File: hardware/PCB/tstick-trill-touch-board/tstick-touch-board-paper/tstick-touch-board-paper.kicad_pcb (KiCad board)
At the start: 2 copper layers, 113.9 x 28 mm, 12 parts

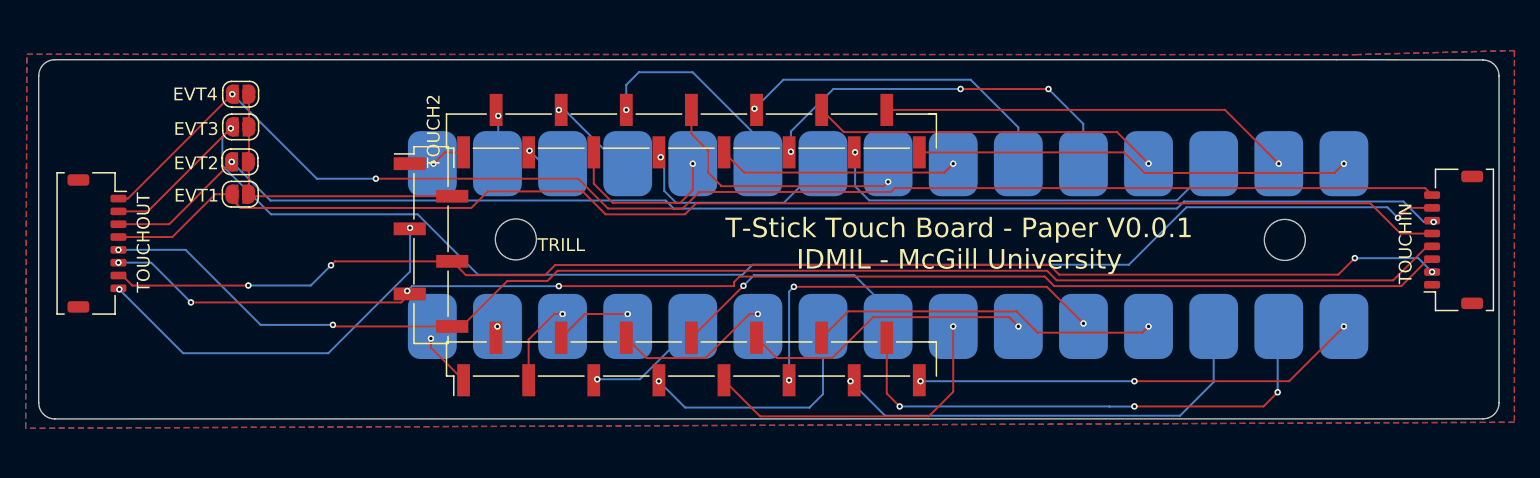
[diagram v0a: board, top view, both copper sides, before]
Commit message: cleaned up the pcb designs for the touch extension boards, created BOM and gerber files for fabrication and assembly
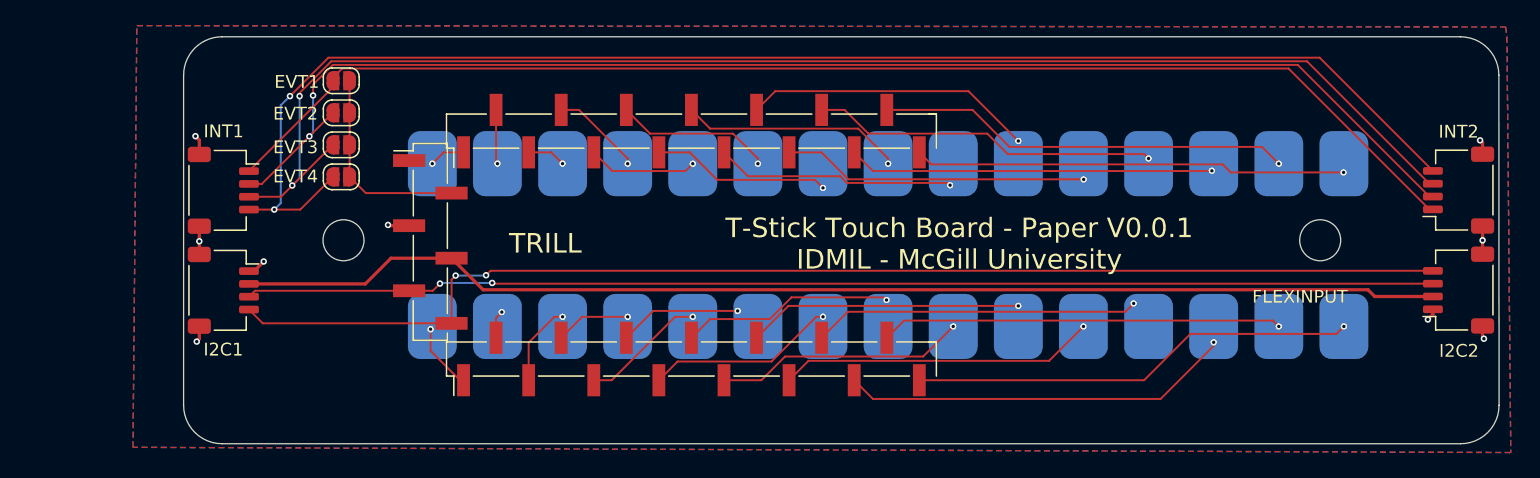
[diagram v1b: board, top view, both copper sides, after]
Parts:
- removed TrillExtensionInput1, TrillExtensionOutput2: Conn_01x08, Connector_JST:JST_SHL_SM08B-SHLS-TF_1x08-1MP_P1.00mm_Horizontal
- added I2C1: Conn_01x04, Connector_JST:JST_SH_SM04B-SRSS-TB_1x04-1MP_P1.00mm_Horizontal, F.Cu at (108.8, 97.2)
- added I2C2: Conn_01x04, Connector_JST:JST_SH_SM04B-SRSS-TB_1x04-1MP_P1.00mm_Horizontal, F.Cu at (205.1, 97.1)
- added INT1: Conn_01x04, Connector_JST:JST_SH_SM04B-SRSS-TB_1x04-1MP_P1.00mm_Horizontal, F.Cu at (108.8, 89.3)
- added INT2: Conn_01x04, Connector_JST:JST_SH_SM04B-SRSS-TB_1x04-1MP_P1.00mm_Horizontal, F.Cu at (205.1, 89.3)
- moved H1 13.4 mm to (118.2, 93.2)
- moved JP1 11.8 mm to (118.0, 80.8)
- moved JP4 10.2 mm to (118.0, 88.3)
- moved JP2 8.78 mm to (118.0, 83.3)
- moved JP3 7.97 mm to (118.0, 85.8)
- moved H2 2.76 mm to (194.3, 93.2)
- moved TRILL1 0.25 mm to (124.9, 93.4)
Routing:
- net GND: track 31.0 -> 13.5 mm, vias 2 -> 9
- net /SDA: track 106.1 -> 92.8 mm, vias 4 -> 2
- net /SCL: track 108.2 -> 96.5 mm
- net +3V3: track 105.7 -> 94.4 mm, vias 4 -> 0
- net /TOUCH13: track 40.9 -> 31.3 mm, vias 3 -> 1
- net /TRILL_EVT: track 23.2 -> 16.0 mm
- net /TOUCH10: track 31.2 -> 24.7 mm, vias 3 -> 1
- net /EVT1: track 107.2 -> 100.7 mm
- net /EVT3: track 115.5 -> 109.1 mm
- net /TOUCH19: track 30.2 -> 23.9 mm, vias 3 -> 1
- net /TOUCH8: track 24.9 -> 19.6 mm
- net /TOUCH25: track 13.3 -> 8.57 mm
- net /TOUCH6: track 19.5 -> 14.9 mm
- net /TOUCH12: track 35.2 -> 30.6 mm
- net /TOUCH24: track 16.8 -> 12.2 mm
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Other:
- board size 113.9 x 28 mm -> 102.6 x 31.8 mm
- board text added: "Center X = 118.75 Y = 92.2625"
- board text added: "FLEXINPUT"
- board text removed: "TOUCHIN"
- board text removed: "TOUCHOUT"
